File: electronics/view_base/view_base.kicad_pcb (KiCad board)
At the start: 2 copper layers, 81.2 x 81.2 mm, 92 parts, among them J1 BLDC, J2 USB_C_Receptacle_USB2.0, J3 LCD, J4 A, J5 B, Q1 MMBT4403, Q2 UMH3N, U1 MT6701-CT, U2 T-Micro32_Plus, U3 CH340C, U4 HX711, U5 TMC6300, U6 AP1117-33, U7 SN74LV1T34DBV, U8 VEML7700

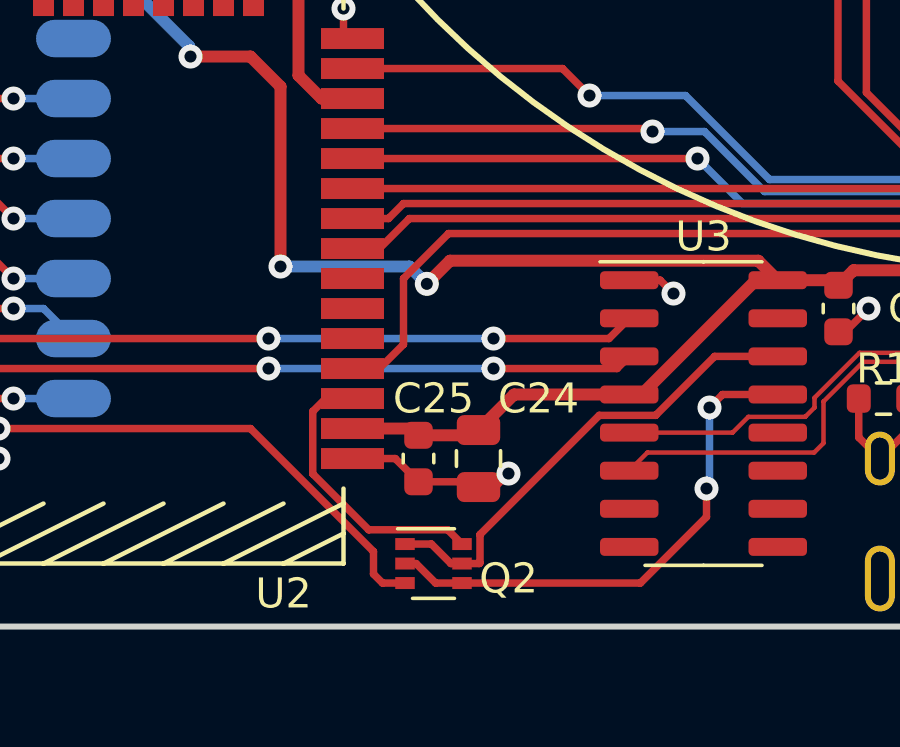
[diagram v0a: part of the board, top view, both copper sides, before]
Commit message: Add EN pullup, capacitor, test points
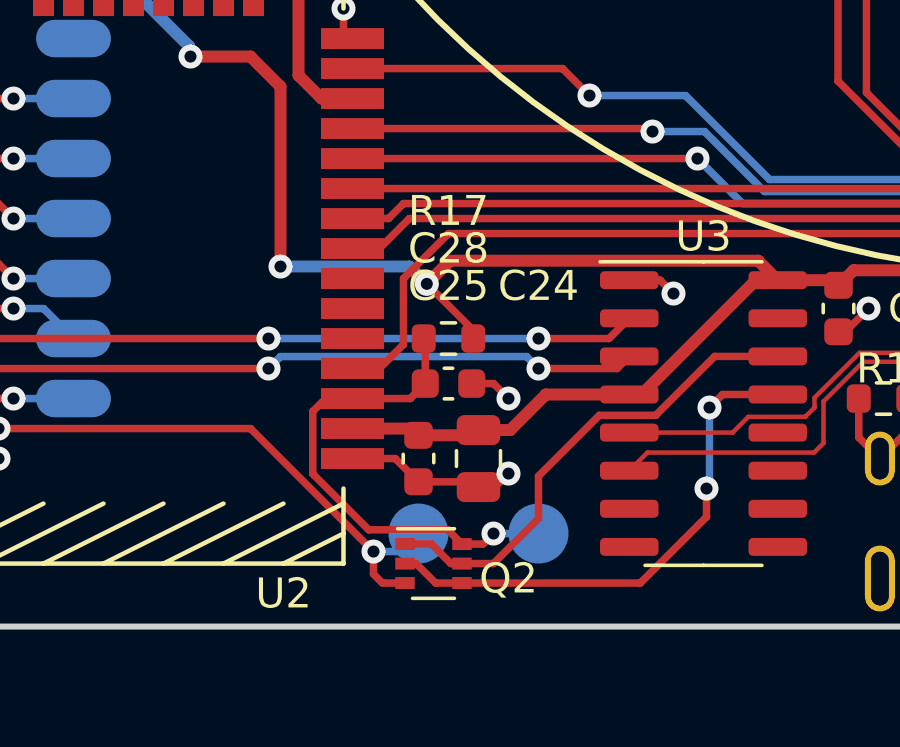
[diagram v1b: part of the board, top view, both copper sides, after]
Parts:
- added C28: 1uF, Capacitor_SMD:C_0603_1608Metric, F.Cu at (-20.0, 32.5)
- added R17: 10k, Resistor_SMD:R_0603_1608Metric, F.Cu at (-20.0, 31.0)
- added TP13: EN, Modified:TestPoint_Pad_D2.0mm_ValueSilk, B.Cu at (-17.0, 37.5)
- added TP14: BOOT, Modified:TestPoint_Pad_D2.0mm_ValueSilk, B.Cu at (-21.0, 37.5)
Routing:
- net /ESP32_EN: track 9.23 -> 15.4 mm, vias 0 -> 1
- net +3V3: track 306.4 -> 308.9 mm
- net /ESP32_BOOT: track 33.2 -> 34.9 mm, vias 2 -> 3
- net GND: track 89.3 -> 90.7 mm, vias 85 -> 86

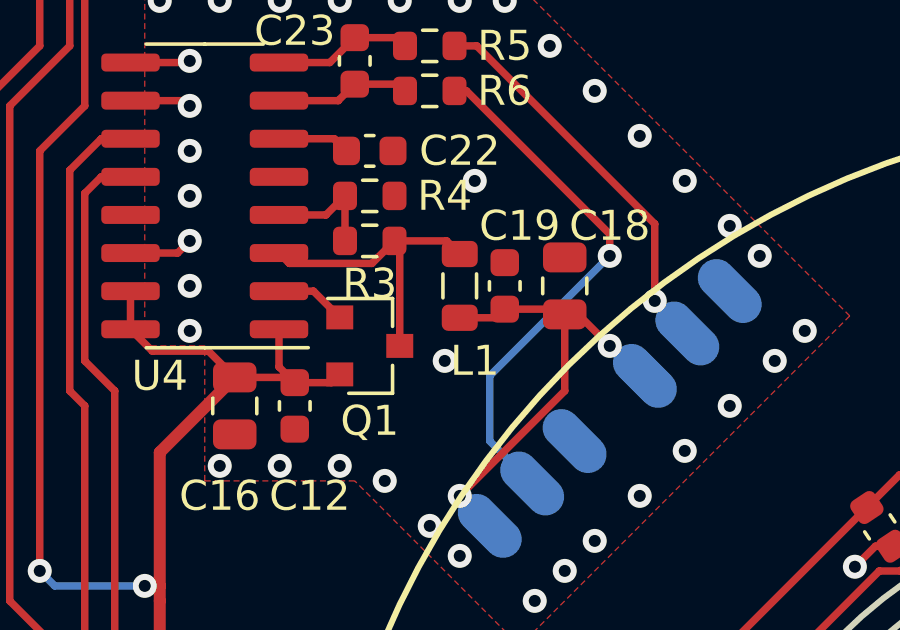
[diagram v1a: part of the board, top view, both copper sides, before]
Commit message: KiBot electronics automation (#1)
Basic KiBot artifact generation - schematic, bom, and pbc renders
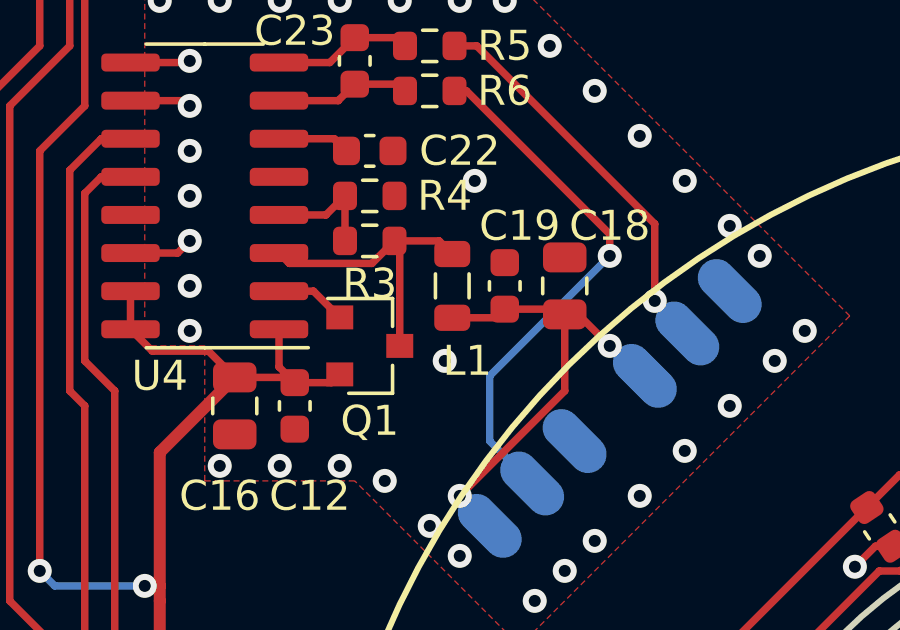
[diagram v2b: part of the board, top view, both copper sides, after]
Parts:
- moved L1 0.25 mm to (-24.2, -23.0)

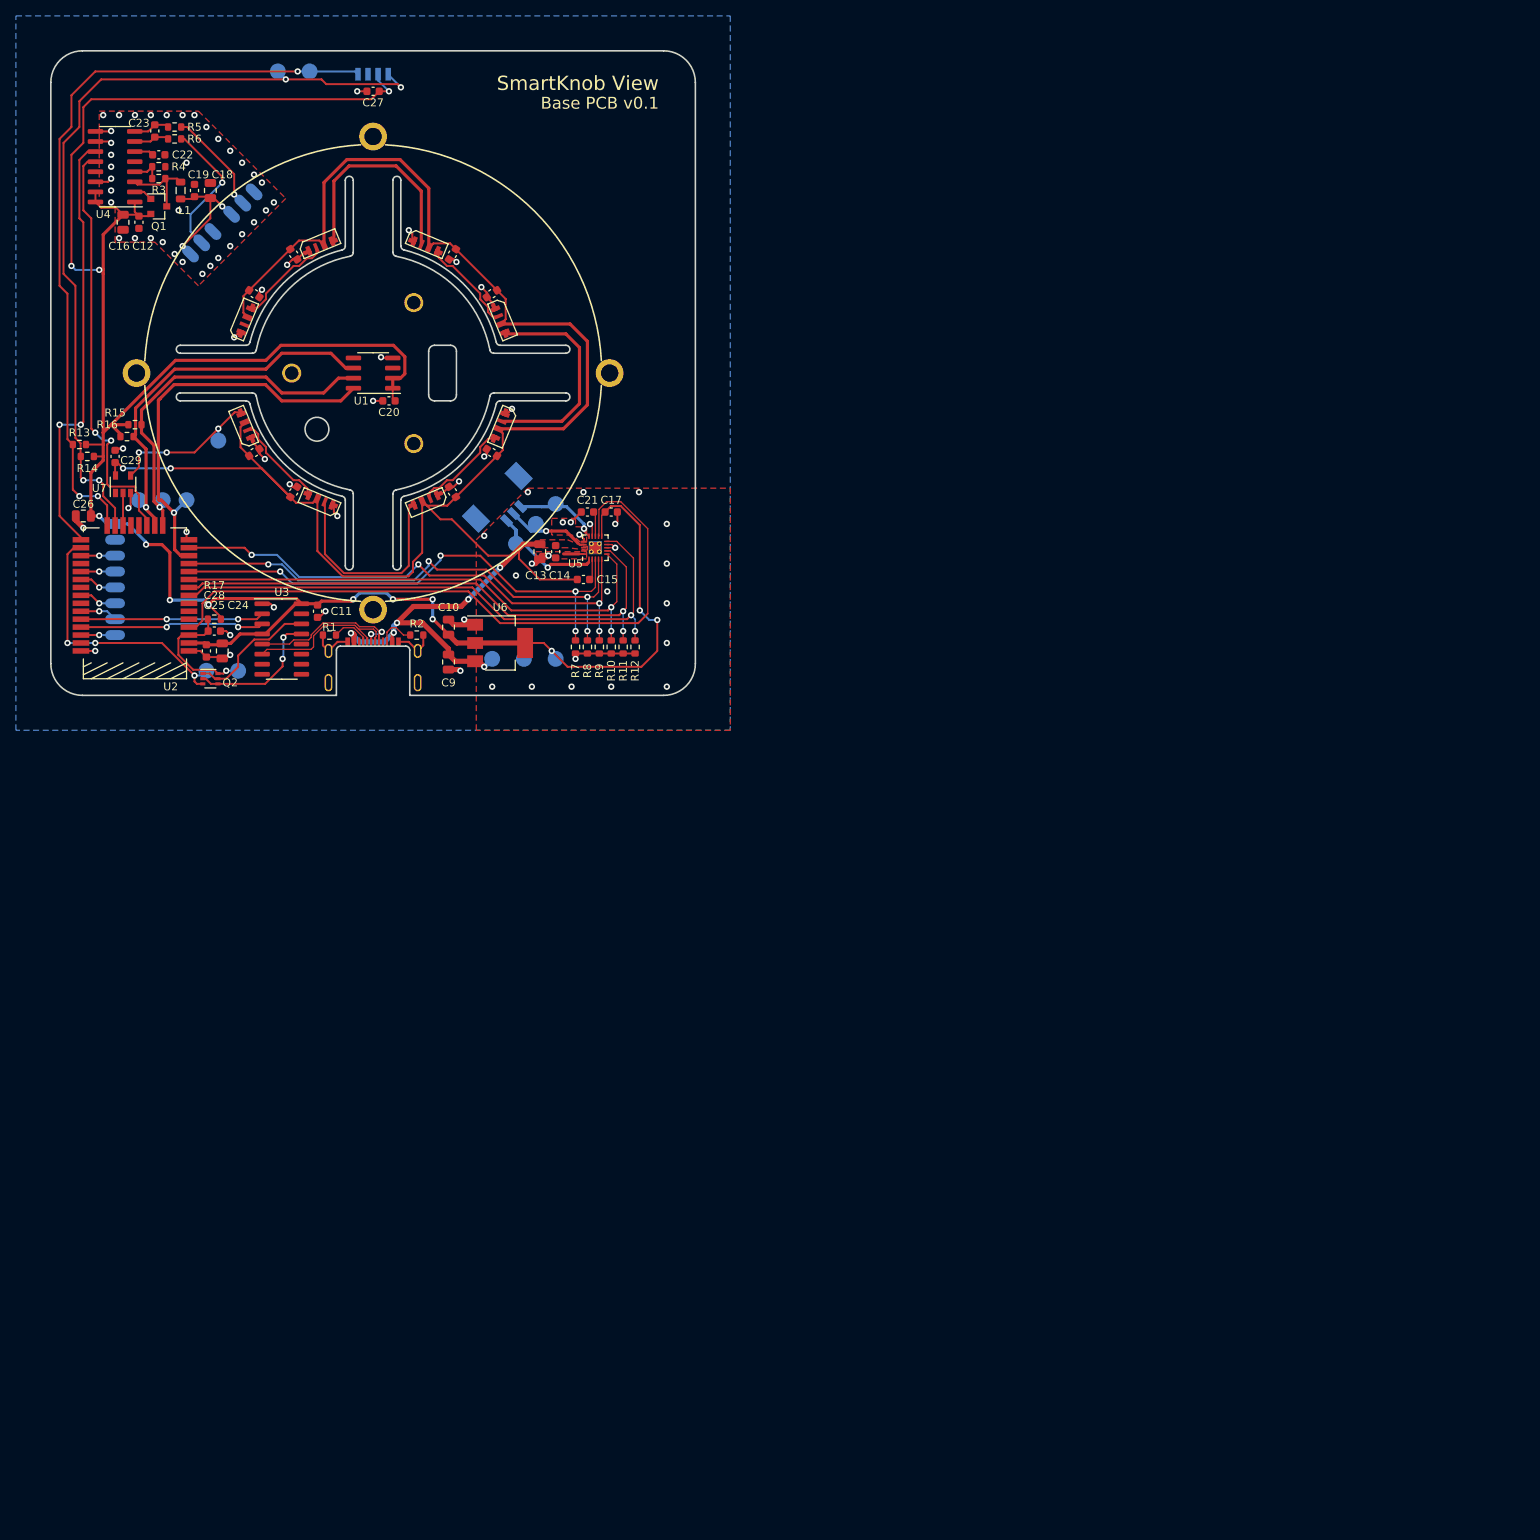
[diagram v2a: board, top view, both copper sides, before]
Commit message: Fab automation (#2)
- Use KiKit for fab automation
- Add splitflap scripts for exporting pcb pdfs, and switch to splitflap script for 3d rendering (for consistency with fab automation)
- Added support in 3d rendering scripts for soldermask & silkscreen colors, option to skip virtual components
- Added silkscreen to base and screen pcbs for commit and date info
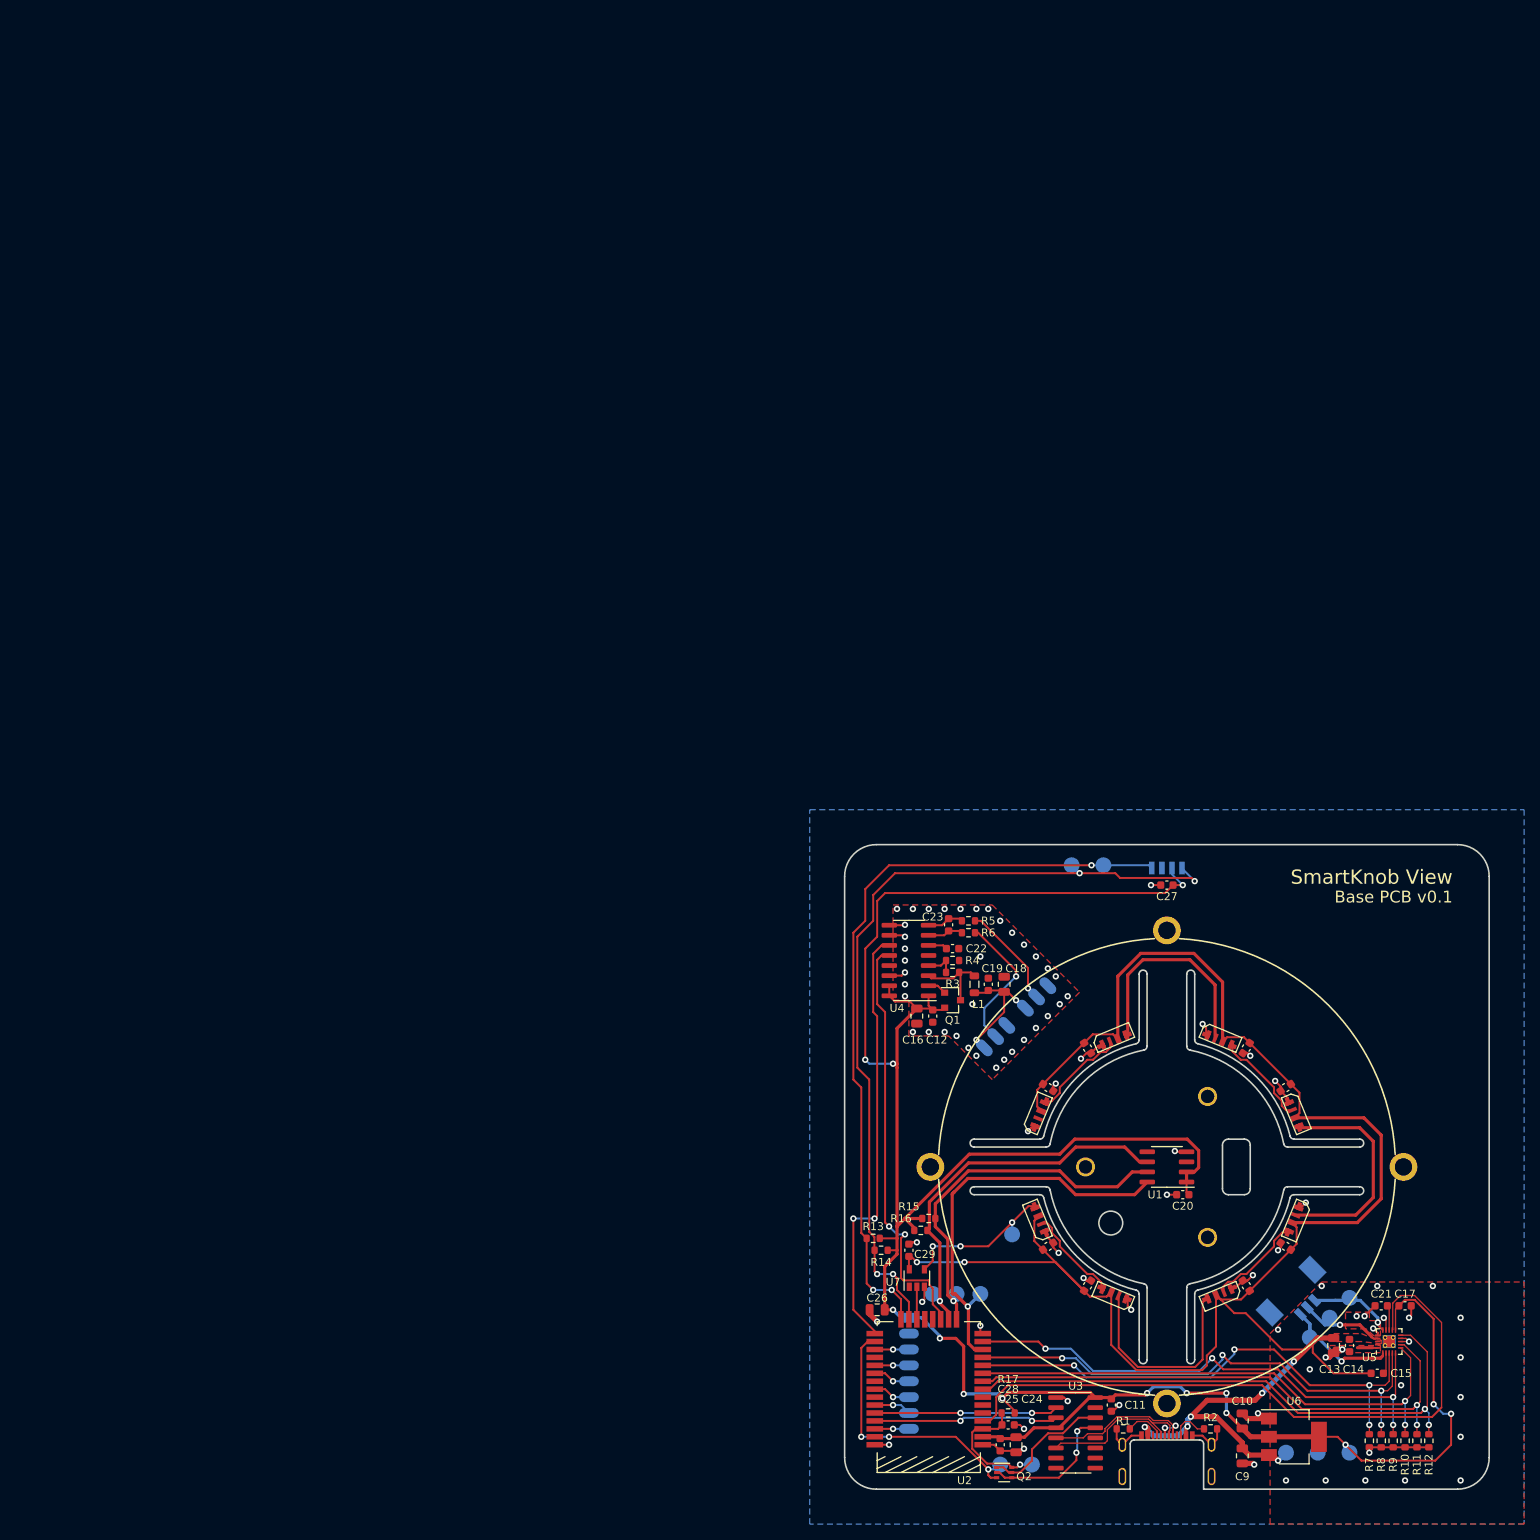
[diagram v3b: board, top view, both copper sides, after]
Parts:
- moved C1 141.4 mm to (85.0, 110.0)
- moved C10 141.4 mm to (109.5, 132.0)
- moved C11 141.4 mm to (93.0, 130.0)
- moved C12 141.4 mm to (70.5, 81.0)
- moved C13 141.4 mm to (121.0, 122.5)
- moved C14 141.4 mm to (123.0, 122.5)
- moved C15 141.4 mm to (126.5, 126.0)
- moved C16 141.4 mm to (68.5, 81.0)
- moved C17 141.4 mm to (130.0, 117.5)
- moved C18 141.4 mm to (79.5, 77.0)
- moved C19 141.4 mm to (77.5, 77.0)
- moved C2 141.4 mm to (90.0, 115.0)
- moved C20 141.4 mm to (102.0, 103.5)
- moved C21 141.4 mm to (127.0, 117.5)
- moved C22 141.4 mm to (73.0, 72.5)
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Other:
- board text added: "DATE: YYYY-MM-DD TIME TZ COMMIT: deadbeef"

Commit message: Remove paste from USB-C pads
USB-C connector will be soldered separately from main top reflow, since it hangs below the board.
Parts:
- J2: footprint GCT_USB:USB4510 -> GCT_USB:USB4510_NoPaste

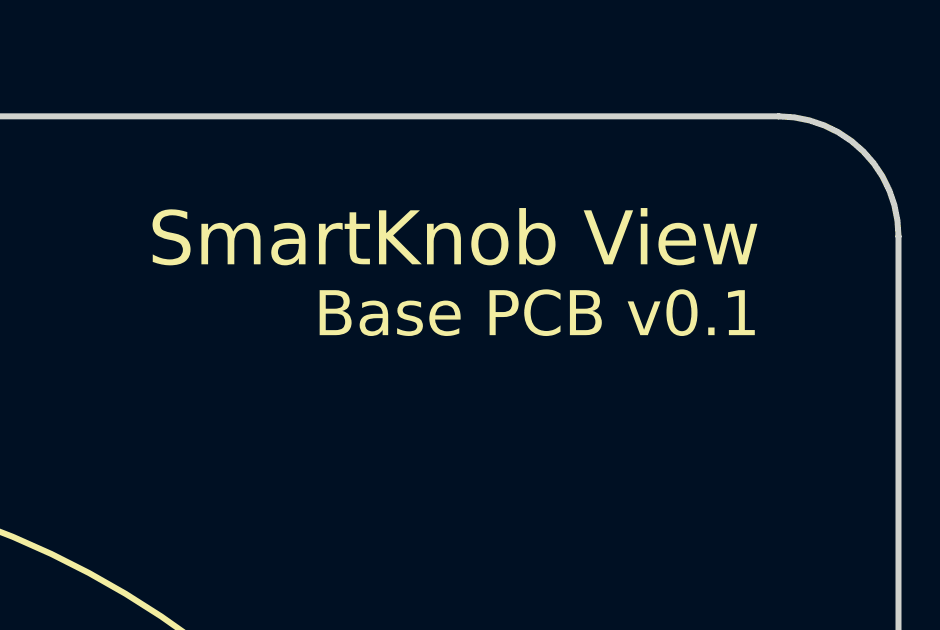
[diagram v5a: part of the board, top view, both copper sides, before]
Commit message: Change View Base to v0.2
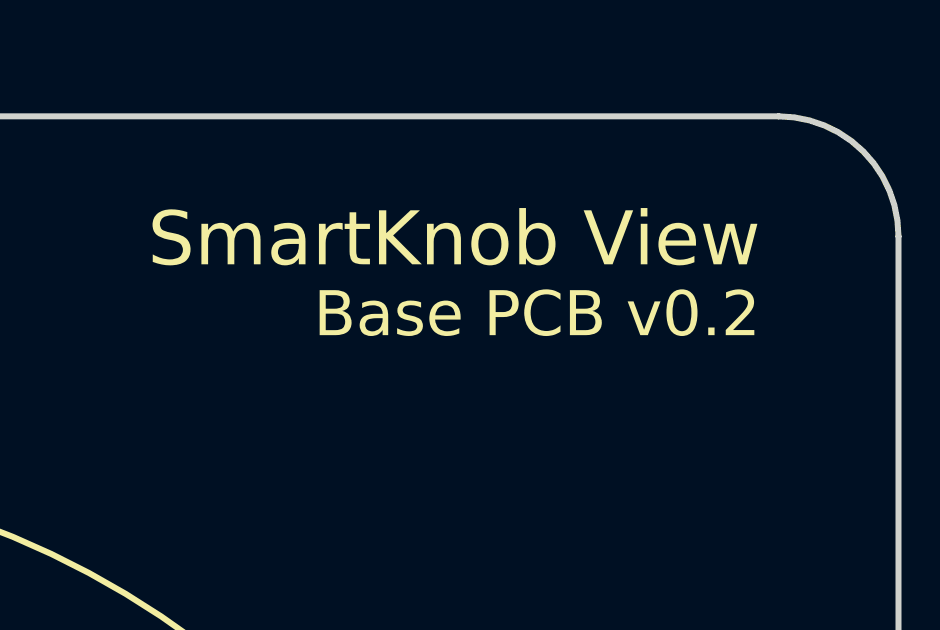
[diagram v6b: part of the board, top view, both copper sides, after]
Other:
- board text added: "Base PCB v0.2"
- board text removed: "Base PCB v0.1"
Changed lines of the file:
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@@
     (effects (font (size 1 1) (thickness 0.15)) (justify mirror))
   )
-  (gr_text "Base PCB v0.1" (at 136 66) (layer F.SilkS)
+  (gr_text "Base PCB v0.2" (at 136 66) (layer F.SilkS)
     (effects (font (size 1.5 1.5) (thickness 0.12)) (justify right))
   )
